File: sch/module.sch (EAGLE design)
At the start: 9 parts

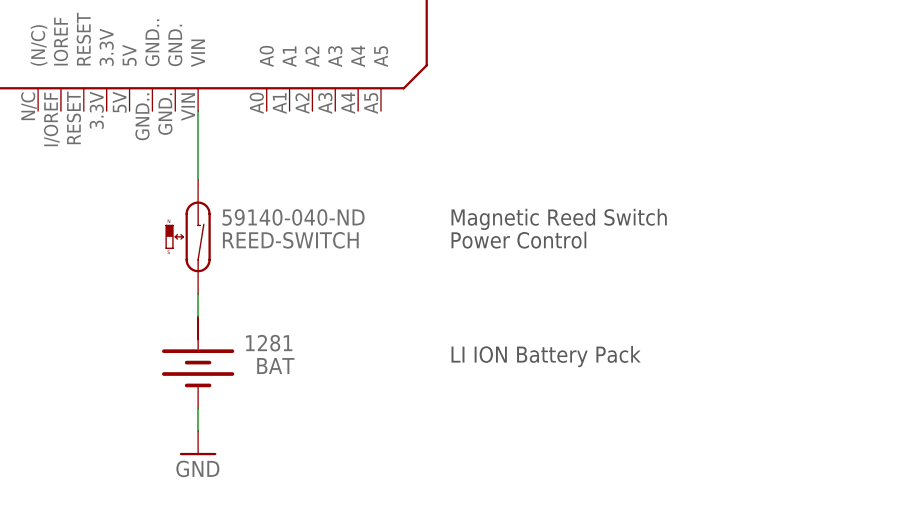
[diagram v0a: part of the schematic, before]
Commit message: Cleaned up schematics, more clearly labeled.
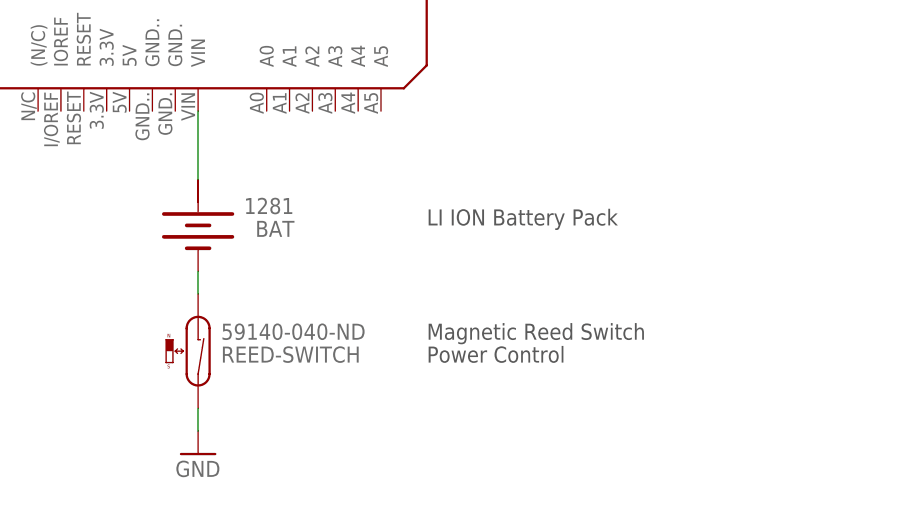
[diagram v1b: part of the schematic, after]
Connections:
- net GND: now also 59140-040-ND.2; no longer 1281.-
- net N$6: now also 1281.+; no longer 59140-040-ND.1
- net N$7: now also 1281.-, 59140-040-ND.1; no longer 1281.+, 59140-040-ND.2
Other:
- moved on the sheet: 1281, 59140-040-ND
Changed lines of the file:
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@@
 <text x="162.56" y="93.98" size="1.778" layer="97">White Button.</text>
 <text x="162.56" y="119.38" size="1.778" layer="97">Red Button</text>
-<text x="137.16" y="5.08" size="1.778" layer="97">Magnetic Reed Switch</text>
-<text x="137.16" y="2.54" size="1.778" layer="97">Power Control</text>
-<text x="137.16" y="-10.16" size="1.778" layer="97">LI ION Battery Pack</text>
+<text x="134.62" y="-7.62" size="1.778" layer="97">Magnetic Reed Switch</text>
+<text x="134.62" y="-10.16" size="1.778" layer="97">Power Control</text>
+<text x="134.62" y="5.08" size="1.778" layer="97">LI ION Battery Pack</text>
 <text x="162.56" y="73.66" size="1.778" layer="97">Status Indicator LED</text>
 </plain>
@@
 </instance>
 <instance part="82T9863" gate="G$1" x="149.86" y="73.66" rot="R90"/>
-<instance part="1281" gate="G$1" x="109.22" y="-10.16" smashed="yes" rot="R270">
-<attribute name="NAME" x="114.3" y="-8.89" size="1.778" layer="95"/>
-<attribute name="VALUE" x="115.57" y="-11.43" size="1.778" layer="96"/>
+<instance part="1281" gate="G$1" x="109.22" y="5.08" smashed="yes" rot="R270">
+<attribute name="NAME" x="114.3" y="6.35" size="1.778" layer="95"/>
+<attribute name="VALUE" x="115.57" y="3.81" size="1.778" layer="96"/>
 </instance>
-<instance part="59140-040-ND" gate="G$1" x="109.22" y="2.54"/>
+<instance part="59140-040-ND" gate="G$1" x="109.22" y="-10.16"/>
 <instance part="GND2" gate="1" x="109.22" y="-20.32"/>
 <instance part="R1" gate="G$1" x="132.08" y="111.76"/>
@@
 </segment>
 <segment>
-<pinref part="1281" gate="G$1" pin="-"/>
+<pinref part="59140-040-ND" gate="G$1" pin="2"/>
 <pinref part="GND2" gate="1" pin="GND"/>
 <wire x1="109.22" y1="-15.24" x2="109.22" y2="-17.78" width="0.1524" layer="91"/>
-</segment>
-</net>
-<net name="N$6" class="0">
-<segment>
-<pinref part="PCB1" gate="G$1" pin="VIN"/>
-<pinref part="59140-040-ND" gate="G$1" pin="1"/>
-<wire x1="109.22" y1="17.78" x2="109.22" y2="10.16" width="0.1524" layer="91"/>
-</segment>
-</net>
-<net name="N$7" class="0">
-<segment>
-<pinref part="59140-040-ND" gate="G$1" pin="2"/>
-<pinref part="1281" gate="G$1" pin="+"/>
-<wire x1="109.22" y1="-2.54" x2="109.22" y2="-5.08" width="0.1524" layer="91"/>
 </segment>
 </net>
@@
 </segment>
 </net>
+<net name="N$6" class="0">
+<segment>
+<pinref part="PCB1" gate="G$1" pin="VIN"/>
+<pinref part="1281" gate="G$1" pin="+"/>
+<wire x1="109.22" y1="17.78" x2="109.22" y2="10.16" width="0.1524" layer="91"/>
+</segment>
+</net>
+<net name="N$7" class="0">
+<segment>
+<pinref part="1281" gate="G$1" pin="-"/>
+<pinref part="59140-040-ND" gate="G$1" pin="1"/>
+<wire x1="109.22" y1="0" x2="109.22" y2="-2.54" width="0.1524" layer="91"/>
+</segment>
+</net>
